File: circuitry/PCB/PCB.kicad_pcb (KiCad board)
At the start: 2 copper layers, 65 x 56 mm, 0 parts

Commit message: layout update
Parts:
- added C1: 0.1u, Capacitor_SMD:C_1206_3216Metric_Pad1.33x1.80mm_HandSolder, F.Cu at (194.1, 101.2)
- added C10: 330u, Capacitor_THT:CP_Radial_D8.0mm_P2.50mm, F.Cu at (211.8, 118.7)
- added C11: 330u, Capacitor_THT:CP_Radial_D8.0mm_P2.50mm, F.Cu at (211.8, 128.2)
- added C12: 4.7u, Capacitor_SMD:C_1206_3216Metric_Pad1.33x1.80mm_HandSolder, F.Cu at (167.7, 124.2)
- added C13: 0.1u, Capacitor_SMD:C_1206_3216Metric_Pad1.33x1.80mm_HandSolder, F.Cu at (173.7, 120.8)
- added C14: 4.7u, Capacitor_SMD:C_1206_3216Metric_Pad1.33x1.80mm_HandSolder, F.Cu at (212.2, 85.0)
- added C15: 4.7u, Capacitor_SMD:C_1206_3216Metric_Pad1.33x1.80mm_HandSolder, F.Cu at (206.2, 91.7)
- added C16: 4.7u, Capacitor_SMD:C_1206_3216Metric_Pad1.33x1.80mm_HandSolder, F.Cu at (173.7, 104.1)
- added C17: 330u, Capacitor_THT:CP_Radial_D8.0mm_P2.50mm, F.Cu at (192.4, 118.7)
- added C18: 330u, Capacitor_THT:CP_Radial_D8.0mm_P2.50mm, F.Cu at (199.1, 138.2)
- added C19: 0.1u, Capacitor_SMD:C_1206_3216Metric_Pad1.33x1.80mm_HandSolder, F.Cu at (179.8, 118.0)
- added C2: 0.1u, Capacitor_SMD:C_1206_3216Metric_Pad1.33x1.80mm_HandSolder, F.Cu at (182.1, 94.5)
- added C20: 4.7u, Capacitor_SMD:C_1206_3216Metric_Pad1.33x1.80mm_HandSolder, F.Cu at (173.7, 107.5)
- added C21: 4.7u, Capacitor_SMD:C_1206_3216Metric_Pad1.33x1.80mm_HandSolder, F.Cu at (215.9, 75.5)
- added C22: 4.7u, Capacitor_SMD:C_1206_3216Metric_Pad1.33x1.80mm_HandSolder, F.Cu at (173.7, 110.8)
- added C23: 0.1u, Capacitor_SMD:C_1206_3216Metric_Pad1.33x1.80mm_HandSolder, F.Cu at (165.2, 130.9)
- added C24: 330u, Capacitor_THT:CP_Radial_D8.0mm_P2.50mm, F.Cu at (187.8, 136.4)
- added C25: 330u, Capacitor_THT:CP_Radial_D8.0mm_P2.50mm, F.Cu at (202.1, 118.7)
- added C26: 0.1u, Capacitor_SMD:C_1206_3216Metric_Pad1.33x1.80mm_HandSolder, F.Cu at (194.1, 97.9)
- added C27: 4.7u, Capacitor_SMD:C_1206_3216Metric_Pad1.33x1.80mm_HandSolder, F.Cu at (173.7, 124.2)
- added C28: 4.7u, Capacitor_SMD:C_1206_3216Metric_Pad1.33x1.80mm_HandSolder, F.Cu at (179.8, 111.3)
- added C29: 4.7u, Capacitor_SMD:C_1206_3216Metric_Pad1.33x1.80mm_HandSolder, F.Cu at (206.2, 88.3)
- added C3: 4.7u, Capacitor_SMD:C_1206_3216Metric_Pad1.33x1.80mm_HandSolder, F.Cu at (182.1, 101.2)
- added C30: 4.7u, Capacitor_SMD:C_1206_3216Metric_Pad1.33x1.80mm_HandSolder, F.Cu at (173.7, 117.5)
- added C31: 4.7u, Capacitor_SMD:C_1206_3216Metric_Pad1.33x1.80mm_HandSolder, F.Cu at (221.9, 75.5)
- added C4: 330u, Capacitor_THT:CP_Radial_D8.0mm_P2.50mm, F.Cu at (192.4, 128.2)
- added C5: 330u, Capacitor_THT:CP_Radial_D8.0mm_P2.50mm, F.Cu at (202.1, 128.2)
- added C6: 0.1u, Capacitor_SMD:C_1206_3216Metric_Pad1.33x1.80mm_HandSolder, F.Cu at (167.7, 107.5)
- added C7: 0.1u, Capacitor_SMD:C_1206_3216Metric_Pad1.33x1.80mm_HandSolder, F.Cu at (167.7, 120.8)
- added C8: 0.1u, Capacitor_SMD:C_1206_3216Metric_Pad1.33x1.80mm_HandSolder, F.Cu at (185.8, 108.0)
- added C9: 4.7u, Capacitor_SMD:C_1206_3216Metric_Pad1.33x1.80mm_HandSolder, F.Cu at (167.7, 110.8)
- added J1: K-LC5, Connector_PinSocket_2.54mm:PinSocket_1x05_P2.54mm_Vertical, F.Cu at (171.7, 76.1)
- added J2: ADS1115, Connector_PinSocket_2.54mm:PinSocket_1x10_P2.54mm_Vertical, F.Cu at (167.1, 76.1)
- added J3: I/Q-amp, Connector_PinSocket_2.54mm:PinSocket_1x02_P2.54mm_Vertical, F.Cu at (159.9, 128.9)
- added J4: Raspberry_Pi_2_3, Connector_PinSocket_2.54mm:PinSocket_2x20_P2.54mm_Vertical, B.Cu at (98.4, 84.8)
- added R1: 10k, Resistor_SMD:R_1206_3216Metric_Pad1.30x1.75mm_HandSolder, F.Cu at (200.1, 94.5)
- added R10: 10k, Resistor_SMD:R_1206_3216Metric_Pad1.30x1.75mm_HandSolder, F.Cu at (179.8, 108.0)
- added R11: 10k, Resistor_SMD:R_1206_3216Metric_Pad1.30x1.75mm_HandSolder, F.Cu at (144.0, 123.0)
- added R12: 10k, Resistor_SMD:R_1206_3216Metric_Pad1.30x1.75mm_HandSolder, F.Cu at (173.7, 114.2)
- added R13: 10k, Resistor_SMD:R_1206_3216Metric_Pad1.30x1.75mm_HandSolder, F.Cu at (215.9, 78.8)
- added R14: 10k, Resistor_SMD:R_1206_3216Metric_Pad1.30x1.75mm_HandSolder, F.Cu at (179.8, 114.7)
- added R15: 10k, Resistor_SMD:R_1206_3216Metric_Pad1.30x1.75mm_HandSolder, F.Cu at (206.2, 85.0)
- added R16: 10k, Resistor_SMD:R_1206_3216Metric_Pad1.30x1.75mm_HandSolder, F.Cu at (188.1, 97.9)
- added R17: 10k, Resistor_SMD:R_1206_3216Metric_Pad1.30x1.75mm_HandSolder, F.Cu at (167.7, 104.1)
- added R18: 10k, Resistor_SMD:R_1206_3216Metric_Pad1.30x1.75mm_HandSolder, F.Cu at (167.7, 127.5)
- added R19: 10k, Resistor_SMD:R_1206_3216Metric_Pad1.30x1.75mm_HandSolder, F.Cu at (188.1, 94.5)
- added R2: 10k, Resistor_SMD:R_1206_3216Metric_Pad1.30x1.75mm_HandSolder, F.Cu at (191.8, 104.6)
- added R20: 10k, Resistor_SMD:R_1206_3216Metric_Pad1.30x1.75mm_HandSolder, F.Cu at (185.8, 104.6)
- added R3: 10k, Resistor_SMD:R_1206_3216Metric_Pad1.30x1.75mm_HandSolder, F.Cu at (167.7, 114.2)
- added R4: 10k, Resistor_SMD:R_1206_3216Metric_Pad1.30x1.75mm_HandSolder, F.Cu at (182.1, 97.9)
- added R5: 10k, Resistor_SMD:R_1206_3216Metric_Pad1.30x1.75mm_HandSolder, F.Cu at (200.1, 97.9)
- added R6: 10k, Resistor_SMD:R_1206_3216Metric_Pad1.30x1.75mm_HandSolder, F.Cu at (188.1, 101.2)
- added R7: 1M, Resistor_SMD:R_1206_3216Metric_Pad1.30x1.75mm_HandSolder, F.Cu at (194.1, 94.5)
- added R8: 1M, Resistor_SMD:R_1206_3216Metric_Pad1.30x1.75mm_HandSolder, F.Cu at (167.7, 117.5)
- added R9: 10k, Resistor_SMD:R_1206_3216Metric_Pad1.30x1.75mm_HandSolder, F.Cu at (179.8, 104.6)
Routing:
- added copper zone on B.Cu, net GND

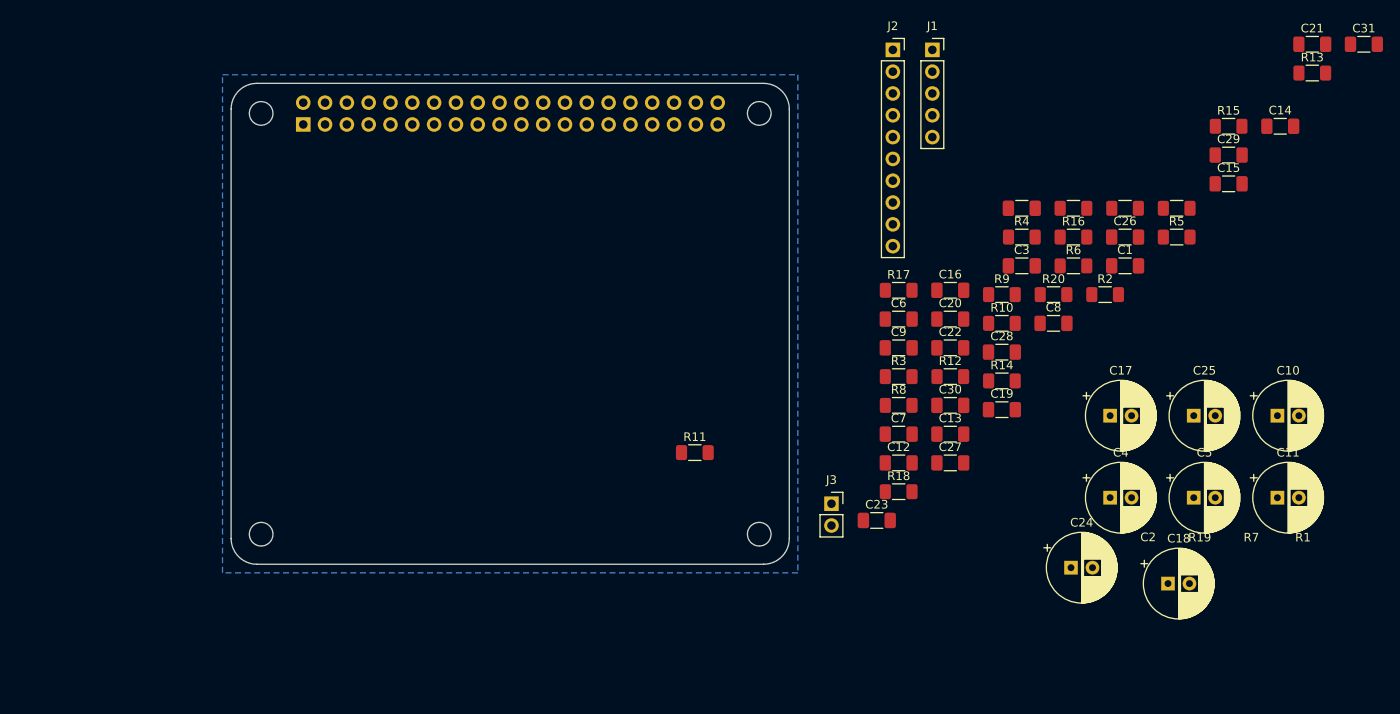
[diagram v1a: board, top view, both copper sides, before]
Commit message: schematic changes, begin board layout
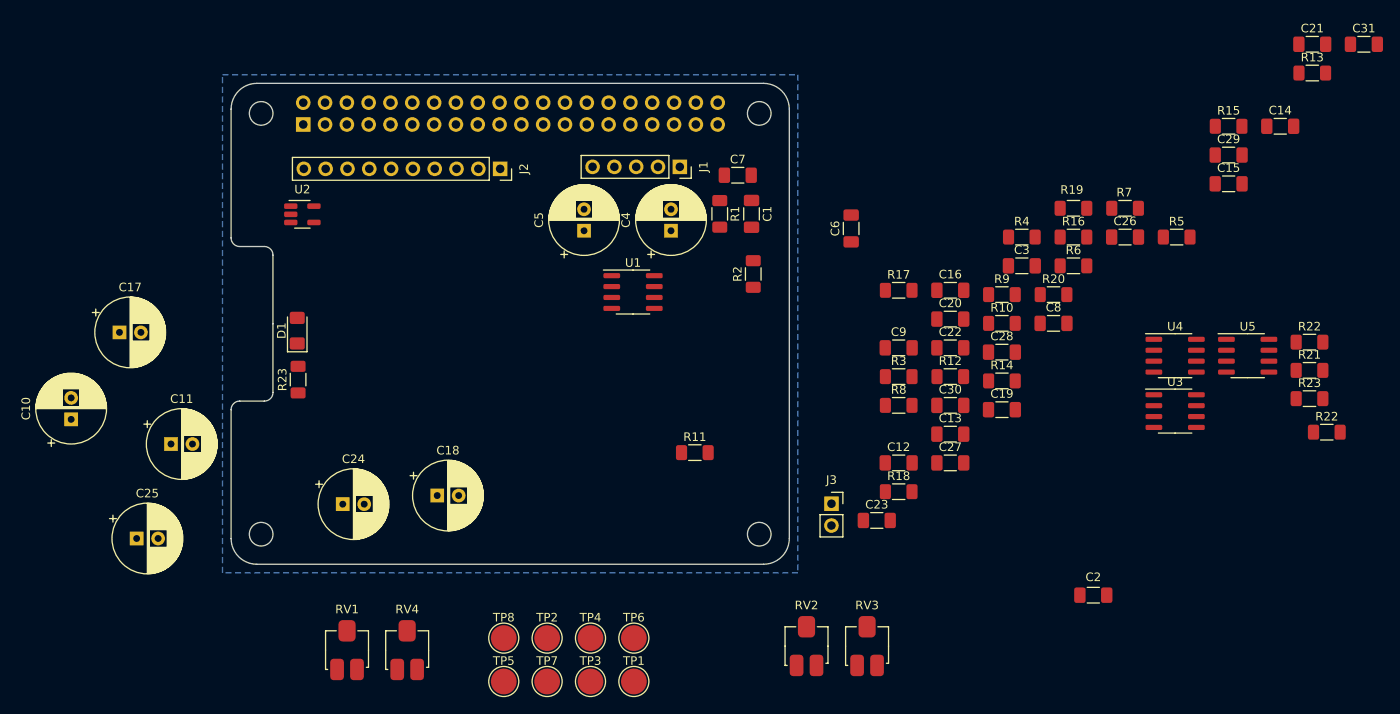
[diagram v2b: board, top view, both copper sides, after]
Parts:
- added D1: RED, LED_SMD:LED_1206_3216Metric_Pad1.42x1.75mm_HandSolder, F.Cu at (97.7, 108.8)
- added R21: 10k, Resistor_SMD:R_1206_3216Metric_Pad1.30x1.75mm_HandSolder, F.Cu at (215.6, 113.4)
- added R22: 20k, Resistor_SMD:R_1206_3216Metric_Pad1.30x1.75mm_HandSolder, F.Cu at (217.6, 120.6)
- added R22: 10k, Resistor_SMD:R_1206_3216Metric_Pad1.30x1.75mm_HandSolder, F.Cu at (215.6, 110.1)
- added R23: 470, Resistor_SMD:R_1206_3216Metric_Pad1.30x1.75mm_HandSolder, F.Cu at (97.8, 114.5)
- added R23: 10k, Resistor_SMD:R_1206_3216Metric_Pad1.30x1.75mm_HandSolder, F.Cu at (215.6, 116.7)
- added RV1: 1M, Proj_Lib:ST4ETA105, F.Cu at (103.5, 146.0)
- added RV2: 1M, Proj_Lib:ST4ETA105, F.Cu at (157.0, 145.5)
- added RV3: 1M, Proj_Lib:ST4ETA105, F.Cu at (164.1, 145.5)
- added RV4: 1M, Proj_Lib:ST4ETA105, F.Cu at (110.5, 146.0)
- added TP1: RV1-2, TestPoint:TestPoint_Pad_D3.0mm, F.Cu at (136.9, 149.7)
- added TP2: RV1-2, TestPoint:TestPoint_Pad_D3.0mm, F.Cu at (126.8, 144.6)
- added TP3: RV1-3, TestPoint:TestPoint_Pad_D3.0mm, F.Cu at (131.8, 149.7)
- added TP4: RV1-3, TestPoint:TestPoint_Pad_D3.0mm, F.Cu at (131.8, 144.6)
- added TP5: RV1-2, TestPoint:TestPoint_Pad_D3.0mm, F.Cu at (121.8, 149.7)
- added TP6: RV1-2, TestPoint:TestPoint_Pad_D3.0mm, F.Cu at (136.9, 144.6)
- added TP7: RV1-3, TestPoint:TestPoint_Pad_D3.0mm, F.Cu at (126.8, 149.7)
- added TP8: RV1-3, TestPoint:TestPoint_Pad_D3.0mm, F.Cu at (121.8, 144.6)
- added U1: MCP6022, Package_SO:SOIC-8_3.9x4.9mm_P1.27mm, F.Cu at (136.8, 104.3)
- added U2: AP2139AK-3.3TRG1, Package_TO_SOT_SMD:SOT-23-5_HandSoldering, F.Cu at (98.3, 95.2)
- added U3: MCP6022, Package_SO:SOIC-8_3.9x4.9mm_P1.27mm, F.Cu at (199.9, 118.2)
- added U4: MCP6022, Package_SO:SOIC-8_3.9x4.9mm_P1.27mm, F.Cu at (199.9, 111.7)
- added U5: MCP6022, Package_SO:SOIC-8_3.9x4.9mm_P1.27mm, F.Cu at (208.4, 111.7)
- C7, C8: value 0.1u -> 4.7u
- moved C10 140.5 mm to (71.4, 119.1), turned to 90 degrees
- moved C11 129.0 mm to (83.0, 122.0)
- moved C25 123.9 mm to (79.0, 133.0)
- moved C17 115.8 mm to (77.0, 109.0)
- moved C18 85.7 mm to (114.0, 128.0)
- moved C24 85.1 mm to (103.0, 129.0)
- moved C5 77.5 mm to (131.1, 97.2), turned to 90 degrees
- moved C4 59.8 mm to (141.2, 97.2), turned to 90 degrees
- moved R1 53.2 mm to (146.9, 95.2), turned to 90 degrees
- moved J2 47.8 mm to (121.3, 90.0), turned to -90 degrees
- moved C2 45.8 mm to (190.4, 139.6)
- moved C1 43.9 mm to (150.6, 95.2), turned to -90 degrees
- moved R2 41.0 mm to (150.8, 102.2), turned to 90 degrees
- moved C7 35.5 mm to (149.0, 90.7)
- moved J1 32.4 mm to (142.2, 89.7), turned to -90 degrees
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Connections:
- J4 pad 6: GND -> unconnected-(J4-Pad6)
- J4 pad 9: unconnected-(J4-Pad9) -> GND
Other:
- outline, holes or cut-outs redrawn

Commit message: just pushing final board design for future reference
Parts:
- removed C16, C27: 4.7u, Capacitor_SMD:C_1206_3216Metric_Pad1.33x1.80mm_HandSolder
- removed the R22 at (215.6, 110.1)
- removed the R23 at (215.6, 116.7)
- added SW1: SW_SPDT, Proj_Lib:PCM12SMTR, F.Cu at (92.1, 93.2)
- C10, C11, C17, C18, C24, C25, C4, C5: footprint Capacitor_THT:CP_Radial_D8.0mm_P2.50mm -> Capacitor_Tantalum_SMD:CP_EIA-3528-12_Kemet-T_Pad1.50x2.35mm_HandSolder
- C3: value 4.7u -> 1u
- I1: renamed from TP1; footprint TestPoint:TestPoint_Pad_D3.0mm -> TestPoint:TestPoint_Pad_D2.5mm
- I2: renamed from TP5; footprint TestPoint:TestPoint_Pad_D3.0mm -> TestPoint:TestPoint_Pad_D2.5mm
- J3: footprint Connector_PinSocket_2.54mm:PinSocket_1x02_P2.54mm_Vertical -> Connector_PinSocket_2.54mm:PinSocket_1x04_P2.54mm_Horizontal
- Q1: renamed from TP2; footprint TestPoint:TestPoint_Pad_D3.0mm -> TestPoint:TestPoint_Pad_D2.5mm
- Q2: renamed from TP6; footprint TestPoint:TestPoint_Pad_D3.0mm -> TestPoint:TestPoint_Pad_D2.5mm
- TP3, TP4, TP7, TP8: footprint TestPoint:TestPoint_Pad_D3.0mm -> TestPoint:TestPoint_Pad_D2.5mm
- moved R22 120.0 mm to (99.1, 101.8)
- moved R21 117.3 mm to (99.1, 99.3), turned to 180 degrees
- moved C31 116.5 mm to (107.3, 96.5), turned to 180 degrees
- moved C21 102.7 mm to (122.0, 117.1), turned to -90 degrees
- moved C29 100.8 mm to (106.1, 100.3), turned to -90 degrees
- moved R13 99.1 mm to (124.5, 117.1), turned to -90 degrees
- moved U5 95.2 mm to (113.9, 100.3), turned to 180 degrees
- moved R15 90.9 mm to (119.2, 111.5), turned to 90 degrees
- moved U4 86.0 mm to (113.9, 111.5), turned to 180 degrees
- moved C3 84.0 mm to (99.1, 88.2)
- moved C26 80.7 mm to (113.9, 106.9)
- moved R16 80.6 mm to (108.6, 111.5), turned to -90 degrees
- moved C10 79.9 mm to (149.0, 100.3)
- moved C2 78.3 mm to (127.2, 93.3), turned to 180 degrees
- moved R20 77.3 mm to (108.6, 100.3), turned to -90 degrees
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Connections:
- C30 pad 1: Q_amp -> I_amp
- C31 pad 1: I_amp -> Q_amp
- C4 pad 2: Q -> I
- C5 pad 2: I -> Q
- J2 pad 7: Q_amp -> I_amp
- J2 pad 8: I_amp -> Q_amp
- J3 pad 1: Q_amp -> I_amp
- J3 pad 2: I_amp -> Q_amp
- J4 pad 14: unconnected-(J4-Pad14) -> GND
- J4 pad 20: unconnected-(J4-Pad20) -> GND
- J4 pad 25: unconnected-(J4-Pad25) -> GND
- J4 pad 30: unconnected-(J4-Pad30) -> GND
- J4 pad 34: unconnected-(J4-Pad34) -> GND
- J4 pad 39: unconnected-(J4-Pad39) -> GND
- J4 pad 4: unconnected-(J4-Pad4) -> 5V
- J4 pad 6: unconnected-(J4-Pad6) -> GND
- U5 pad 1: Q_amp -> I_amp
- U5 pad 2: Q_amp -> I_amp
- U5 pad 6: I_amp -> Q_amp
- U5 pad 7: I_amp -> Q_amp
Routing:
- net VCC: track 0.00 -> 255.3 mm
- net I_amp: track 0.00 -> 51.4 mm, vias 0 -> 2
- net GND: track 0.00 -> 49.5 mm, vias 0 -> 70
- net Net-(R13-Pad2): track 0.00 -> 48.4 mm, vias 0 -> 2
- net Q_amp: track 0.00 -> 47.9 mm
- net Net-(C22-Pad1): track 0.00 -> 38.1 mm, vias 0 -> 2
- net Net-(R17-Pad2): track 0.00 -> 31.5 mm, vias 0 -> 2
- net Net-(R18-Pad2): track 0.00 -> 30.5 mm
- net Net-(Q2-Pad1): track 0.00 -> 28.6 mm
- net Net-(Q1-Pad1): track 0.00 -> 28.4 mm, vias 0 -> 2
- net Net-(C5-Pad1): track 0.00 -> 25.0 mm
- net 5V: track 0.00 -> 23.5 mm
- net Net-(R14-Pad2): track 0.00 -> 22.8 mm
- net Net-(I1-Pad1): track 0.00 -> 21.9 mm
- net Net-(I2-Pad1): track 0.00 -> 19.1 mm
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- added copper zone on F.Cu, net GND
